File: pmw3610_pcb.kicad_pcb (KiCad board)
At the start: 2 copper layers, 23.5 x 31.5 mm, 23 parts, among them J1 Conn_01x06, U1 PMW3610, U2 TLV74318PDBVR

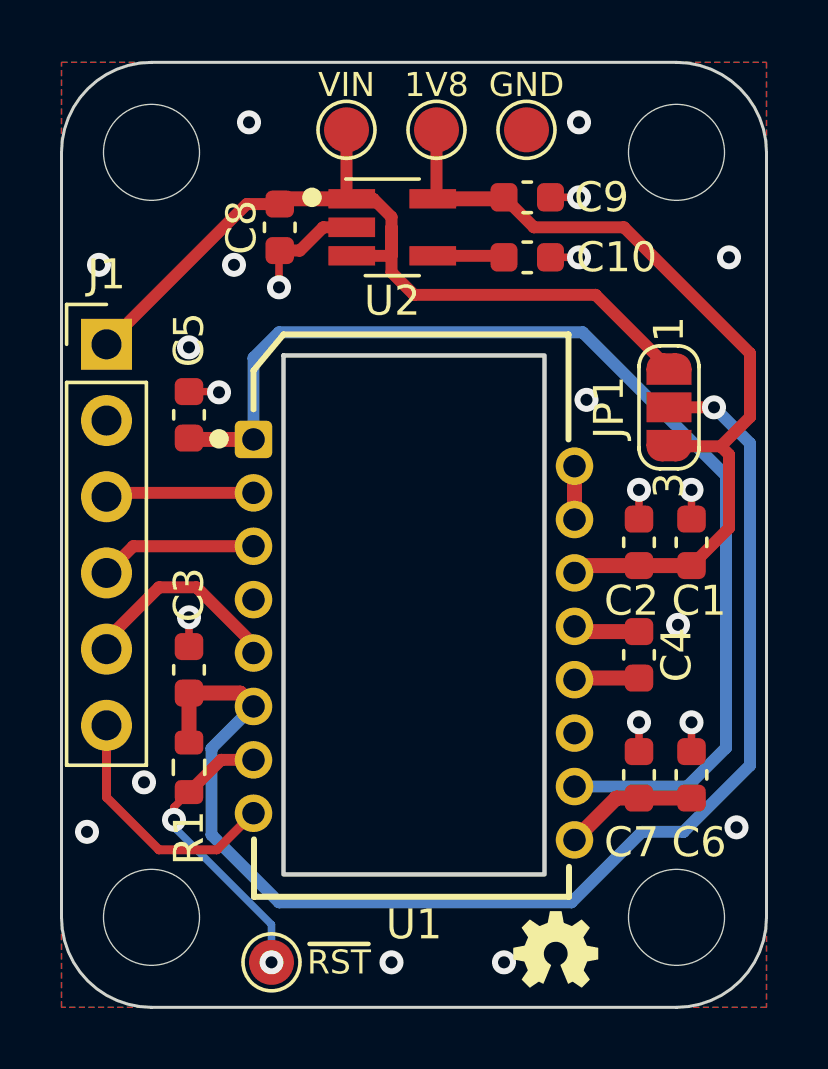
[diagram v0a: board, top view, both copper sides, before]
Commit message: Add `J2` FPC/FFC connecter
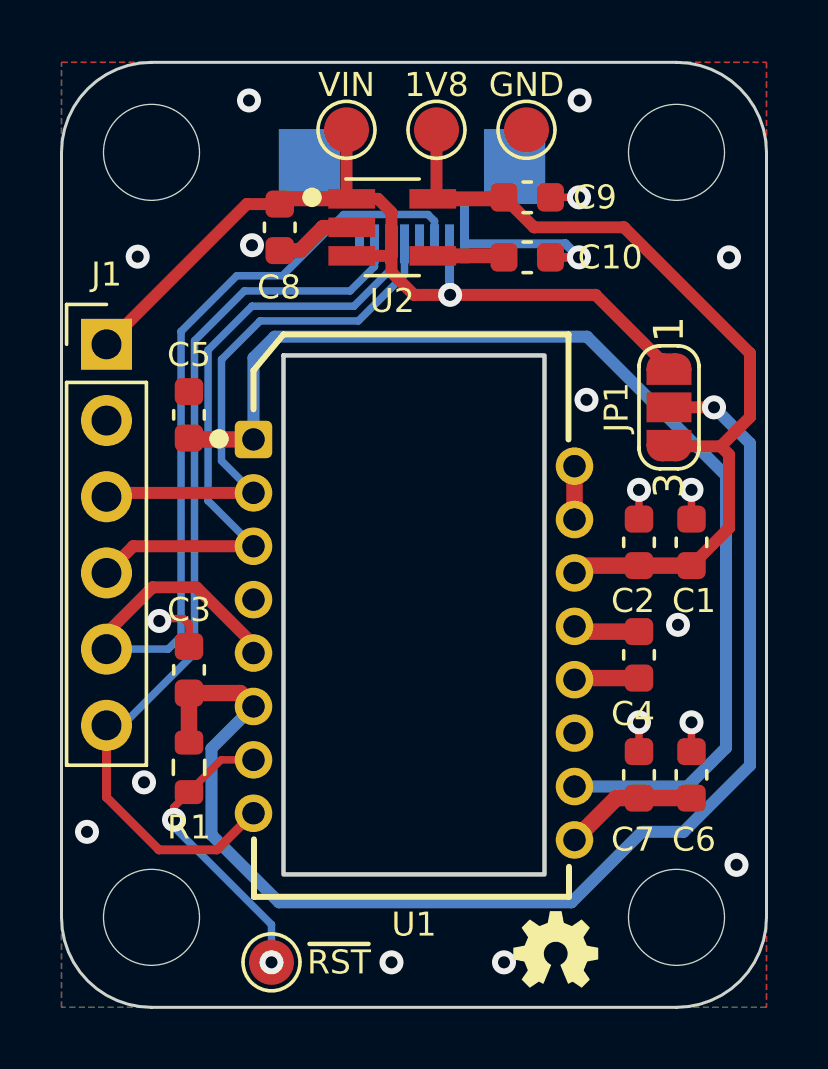
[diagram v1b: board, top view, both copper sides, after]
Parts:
- added J2: Conn_01x08, pmw3610_pcb:FPC_8P_0.5mm_AFC01-S08FCA-00, B.Cu at (149.9, 87.3)
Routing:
- net nCS: track 7.01 -> 30.9 mm
- net MOTION: track 8.53 -> 30.7 mm
- net SCLK: track 5.27 -> 20.5 mm
- net SDIO: track 4.95 -> 18.1 mm
- net GND: track 11.8 -> 15.9 mm, vias 22 -> 19
- net VIN: track 29.1 -> 30.9 mm, vias 0 -> 1
